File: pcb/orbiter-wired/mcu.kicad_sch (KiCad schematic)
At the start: 24 parts, among them J4 AudioJack4, Q2 BSS138, SW30 SW_Push

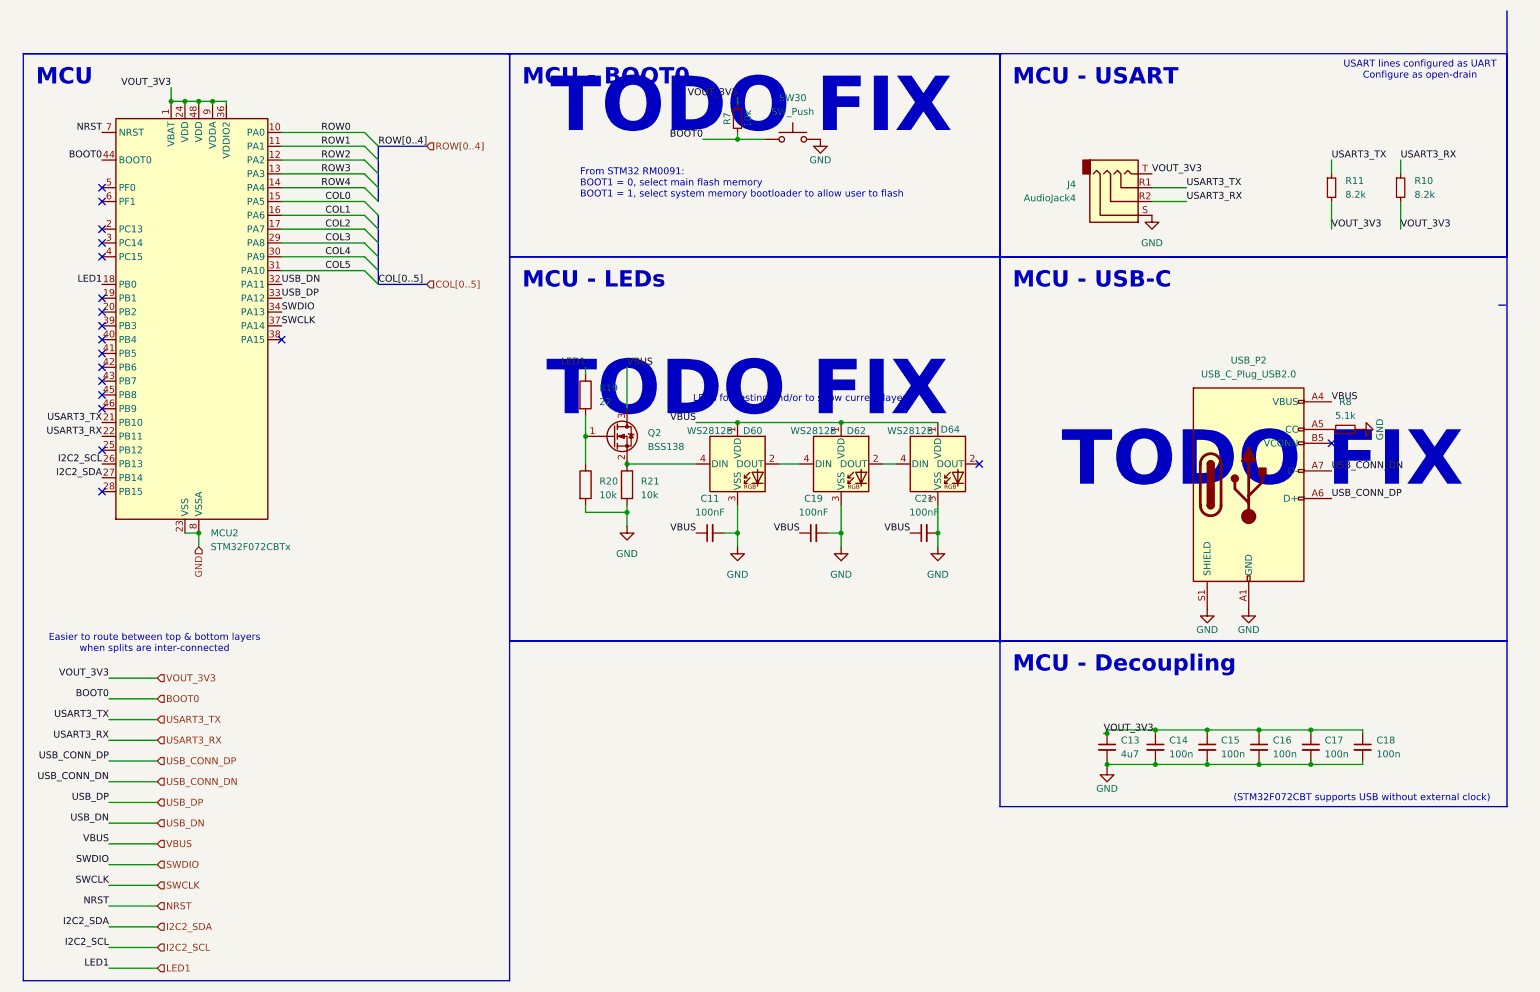
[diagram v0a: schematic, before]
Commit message: Bump to Kicad 9
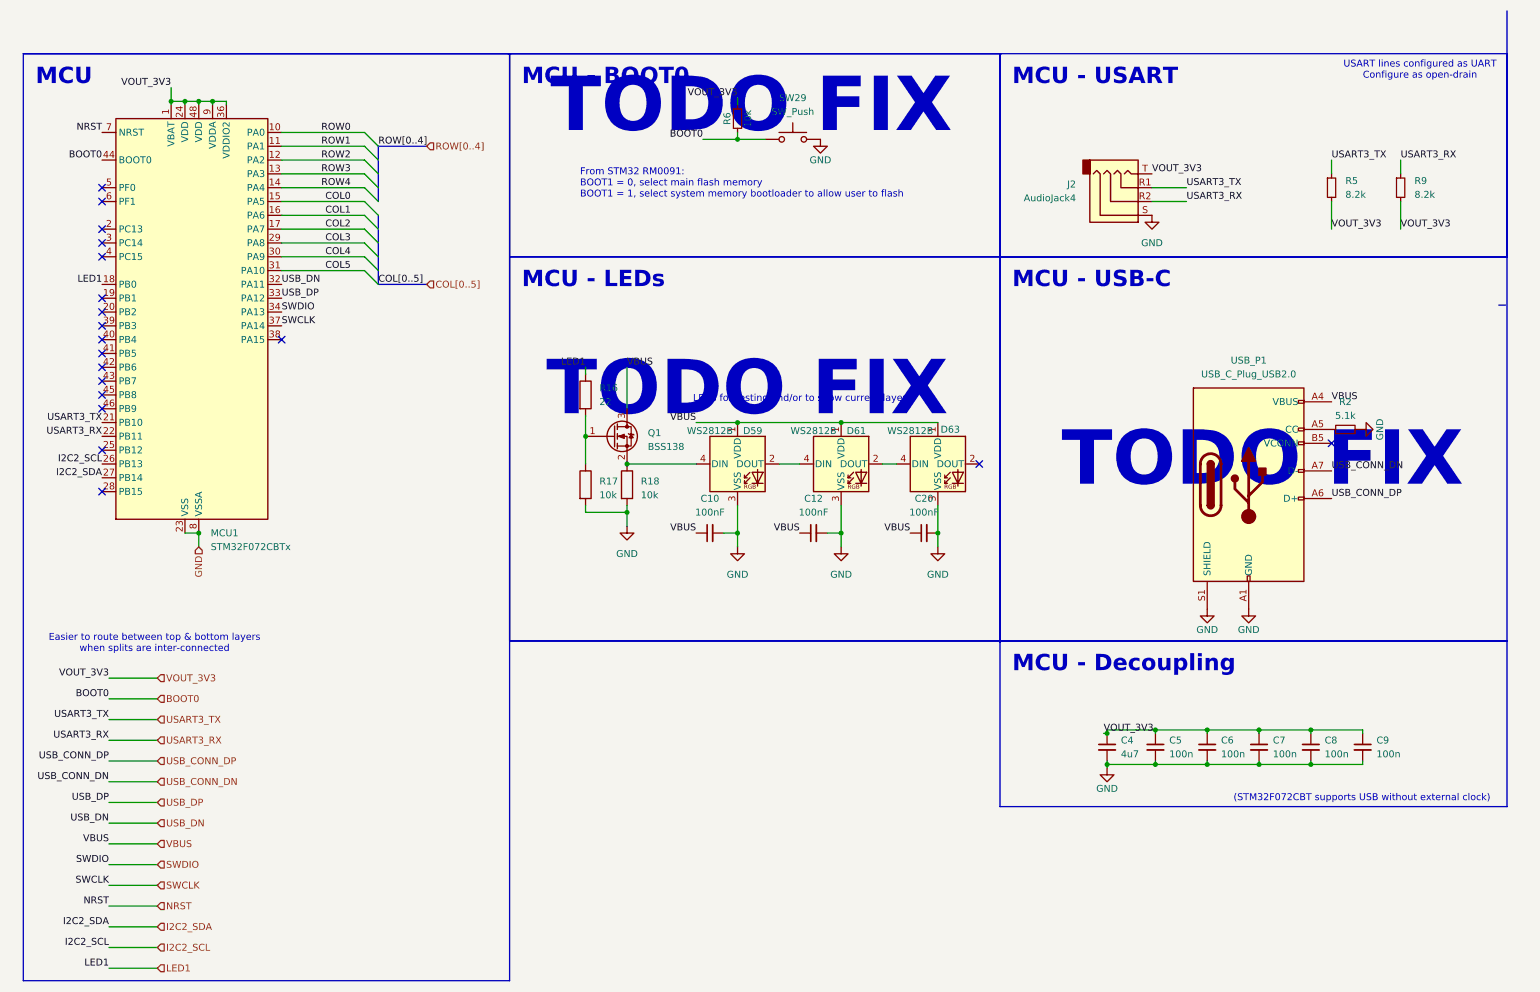
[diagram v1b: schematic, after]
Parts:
- renumbered C11 to C10, C19 to C12, C21 to C20, C13 to C4, C14 to C5, C15 to C6, C16 to C7, C17 to C8, C18 to C9, D60 to D59, D62 to D61, D64 to D63, J4 to J2, MCU2 to MCU1, Q2 to Q1, R19 to R16, R20 to R17, R21 to R18, R8 to R2, R11 to R5, R7 to R6, R10 to R9, SW30 to SW29, USB_P2 to USB_P1

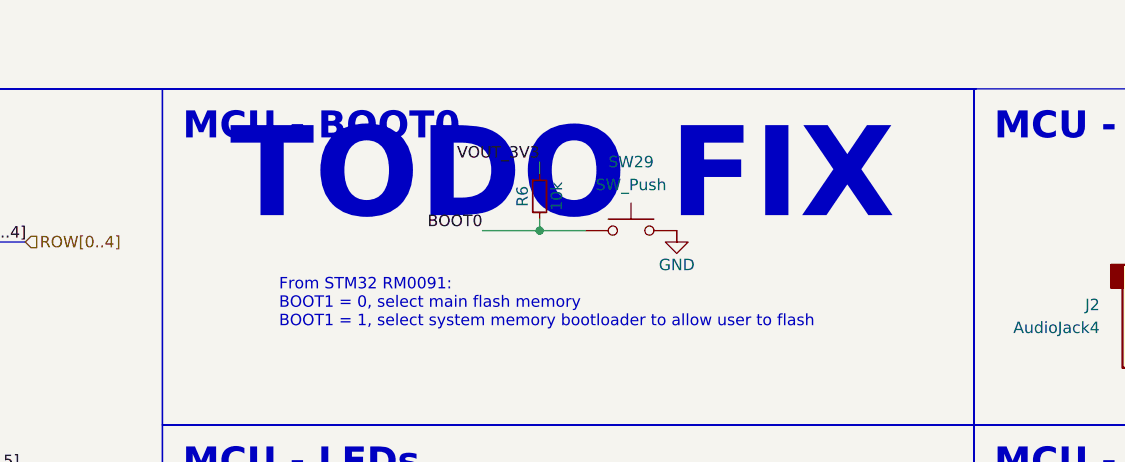
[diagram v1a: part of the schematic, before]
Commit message: fix schema inverted boot0 logic
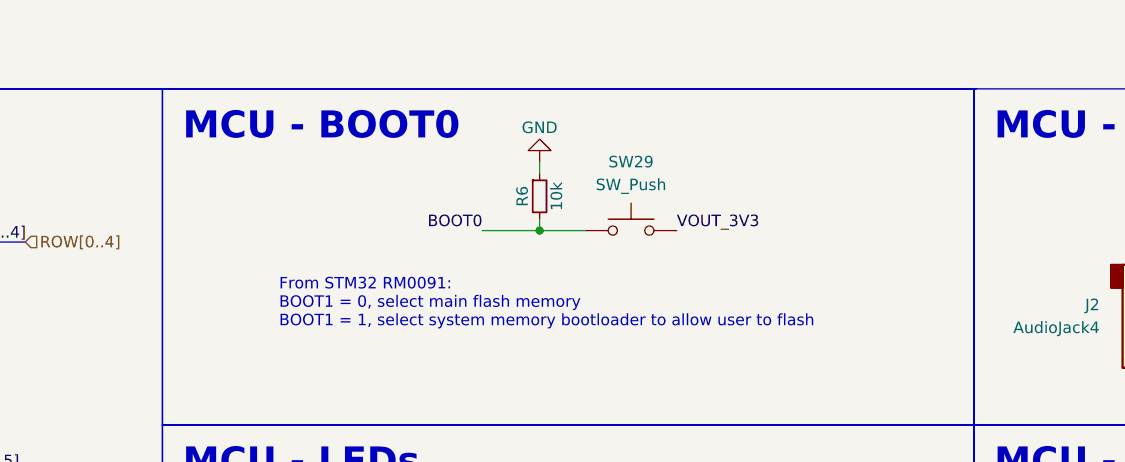
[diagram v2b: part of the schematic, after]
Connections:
- net GND: now also R6.1; no longer SW29.2
- net VOUT_3V3: now also SW29.2; no longer R6.1
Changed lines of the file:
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@@
 		)
 	)
-	(text "TODO FIX"
-		(exclude_from_sim no)
-		(at 146.05 37.084 0)
-		(effects
-			(font
-				(size 10 10)
-				(bold yes)
-			)
-		)
-	)
 	(text "(STM32F072CBT supports USB without external clock)"
 		(exclude_from_sim no)
@@
 	)
 	(label "VOUT_3V3"
+		(at 158.75 43.18 0)
+		(effects
+			(font
+				(size 1.27 1.27)
+			)
+			(justify left bottom)
+		)
+	)
+	(label "VOUT_3V3"
 		(at 39.37 33.655 180)
 		(effects
@@
 		)
 	)
-	(label "VOUT_3V3"
-		(at 143.51 35.56 180)
-		(effects
-			(font
-				(size 1.27 1.27)
-			)
-			(justify right bottom)
-		)
-	)
 	(label "NRST"
 		(at 27.94 184.15 180)
@@
 	(symbol
 		(lib_id "STM32F4_REV2-rescue:GND-power")
-		(at 158.75 43.18 0)
+		(at 143.51 35.56 180)
 		(unit 1)
 		(exclude_from_sim no)
@@
 		(dnp no)
 		(property "Reference" "#PWR012"
-			(at 158.75 49.53 0)
+			(at 143.51 29.21 0)
 			(effects
 				(font
@@
 		)
 		(property "Value" "GND"
-			(at 158.75 46.99 0)
+			(at 143.51 31.75 0)
 			(effects
 				(font
@@
 		)
 		(property "Footprint" ""
-			(at 158.75 43.18 0)
+			(at 143.51 35.56 0)
 			(effects
 				(font
@@
 		)
 		(property "Datasheet" ""
-			(at 158.75 43.18 0)
+			(at 143.51 35.56 0)
 			(effects
 				(font
@@
 		)
 		(property "Description" ""
-			(at 158.75 43.18 0)
+			(at 143.51 35.56 0)
 			(effects
 				(font
@@
 			(project "orbiter"
 				(path "/623f70b3-6381-43ff-98c1-e36c34bee313/c14a50ad-c630-40dd-ac14-b3b40c9c245d"
-					(reference "#PWR018")
+					(reference "#PWR012")
 					(unit 1)
 				)

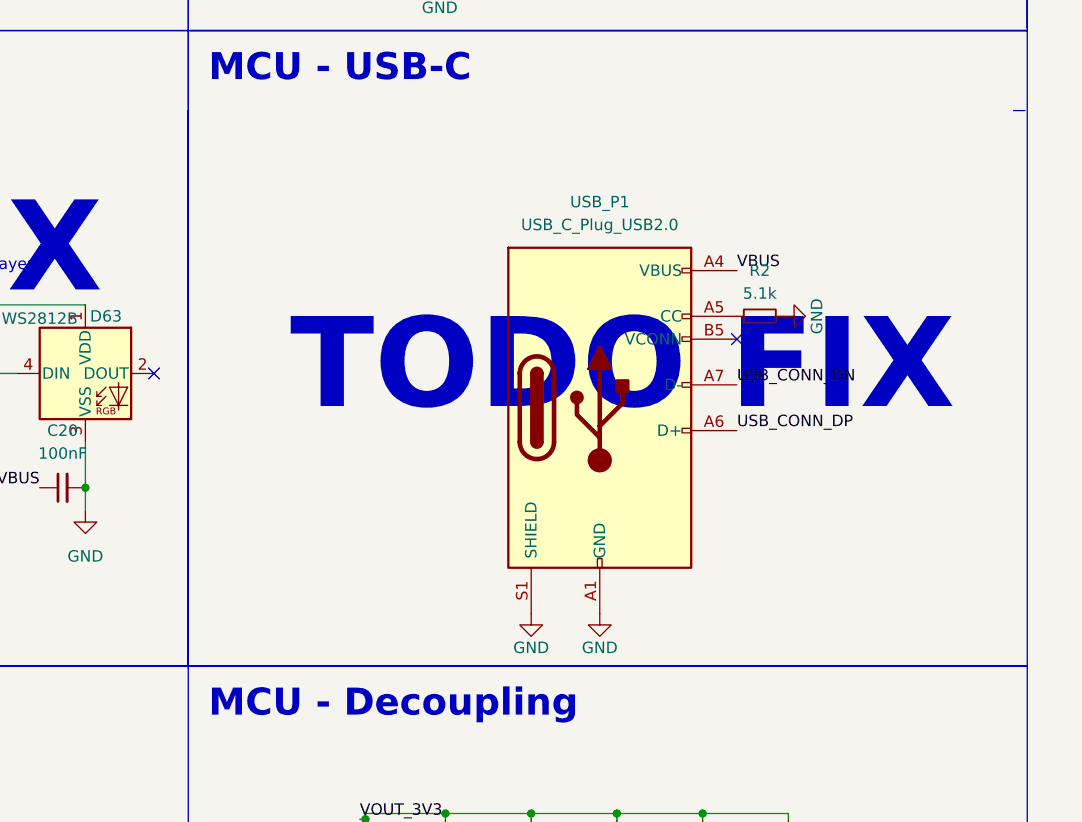
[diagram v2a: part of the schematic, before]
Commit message: update schema to fix USB CC issue and add emc protection
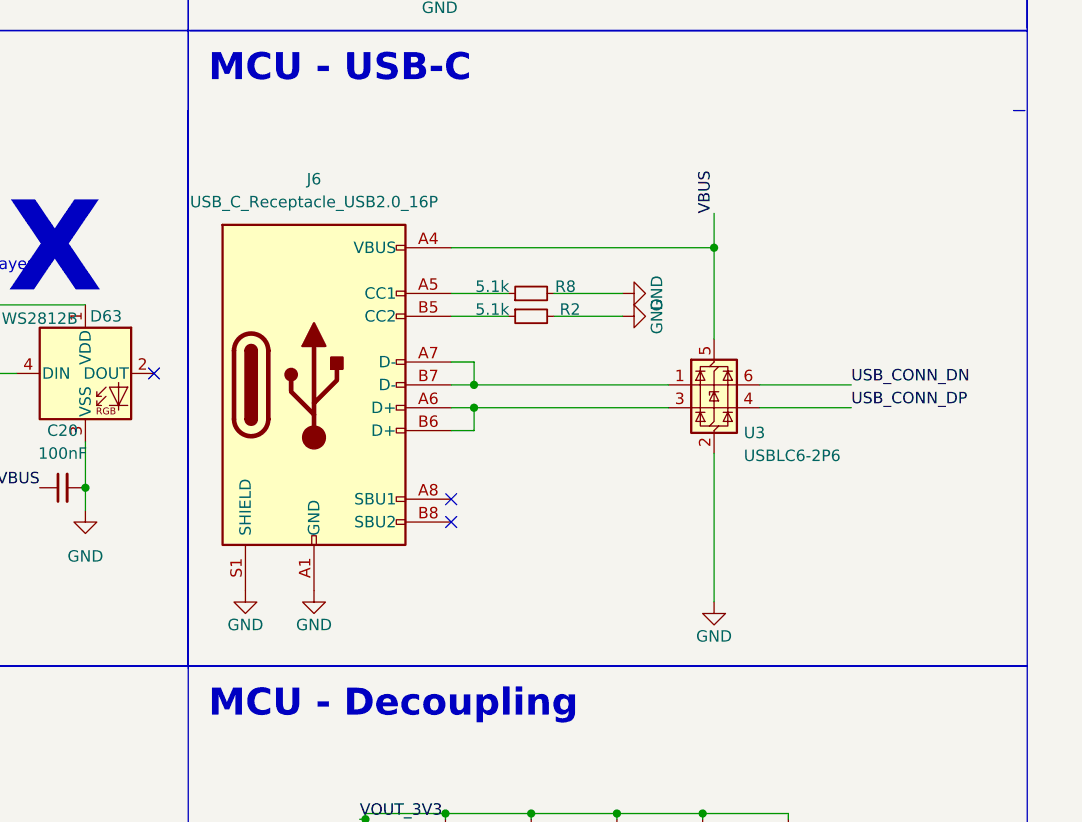
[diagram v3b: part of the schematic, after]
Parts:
- removed USB_P1: USB_C_Plug_USB2.0, Connector_USB:USB_C_Receptacle_XKB_U262-16XN-4BVC11, symbol Connector:USB_C_Plug_USB2.0
- added J6: USB_C_Receptacle_USB2.0_16P, symbol Connector:USB_C_Receptacle_USB2.0_16P
- added R2: 5.1k, Resistor_SMD:R_0603_1608Metric, symbol Device:R_Small
- added U3: USBLC6-2P6, Package_TO_SOT_SMD:SOT-666, symbol Power_Protection:USBLC6-2P6
- renumbered R2 to R8
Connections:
- net GND: now also J6.A1 (GND), J6.A12 (GND), J6.B1 (GND), J6.B12 (GND), J6.S1 (SHIELD), R2.2, U3.2 (GND)
- net USB_CONN_DN: now also U3.6 (I/O1)
- net USB_CONN_DP: now also U3.4 (I/O2)
- net VBUS: now also J6.A4 (VBUS), J6.A9 (VBUS), J6.B4 (VBUS), J6.B9 (VBUS), U3.5 (VBUS)
- net at R8.1: now also J6.A5 (CC1)
- new net: J6.A6 (D+), J6.B6 (D+), U3.3 (I/O2)
- new net: J6.A7 (D-), J6.B7 (D-), U3.1 (I/O1)
- new net: J6.B5 (CC2), R2.1
- no-connect marks 19 -> 20
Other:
- moved on the sheet: R8
